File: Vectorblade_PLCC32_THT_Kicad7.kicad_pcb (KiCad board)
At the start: 2 copper layers, 47.2 x 46.9 mm, 12 parts, among them CON3 EDGE-CONNECTOR, U1 SST39SF020, U2 74AHC1G08, U3 74AHC1G04

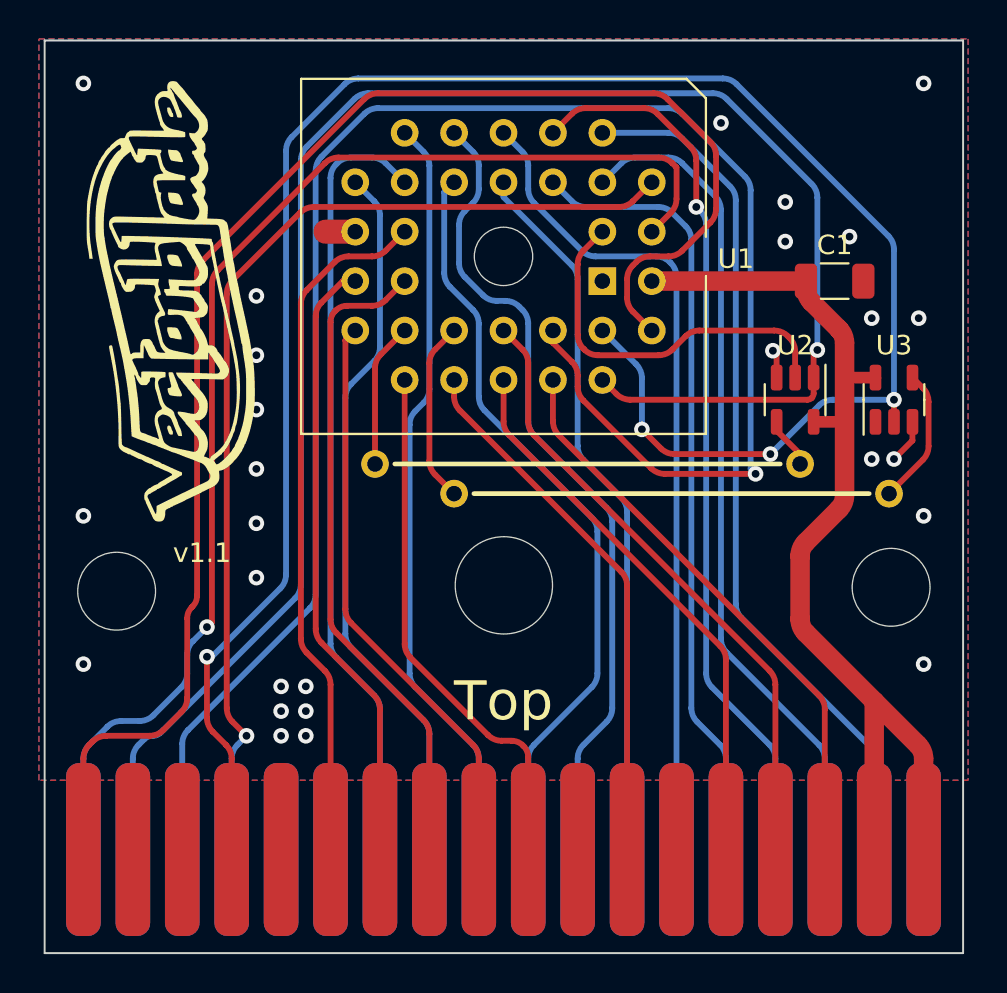
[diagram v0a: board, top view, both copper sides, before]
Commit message: Correct a roud track
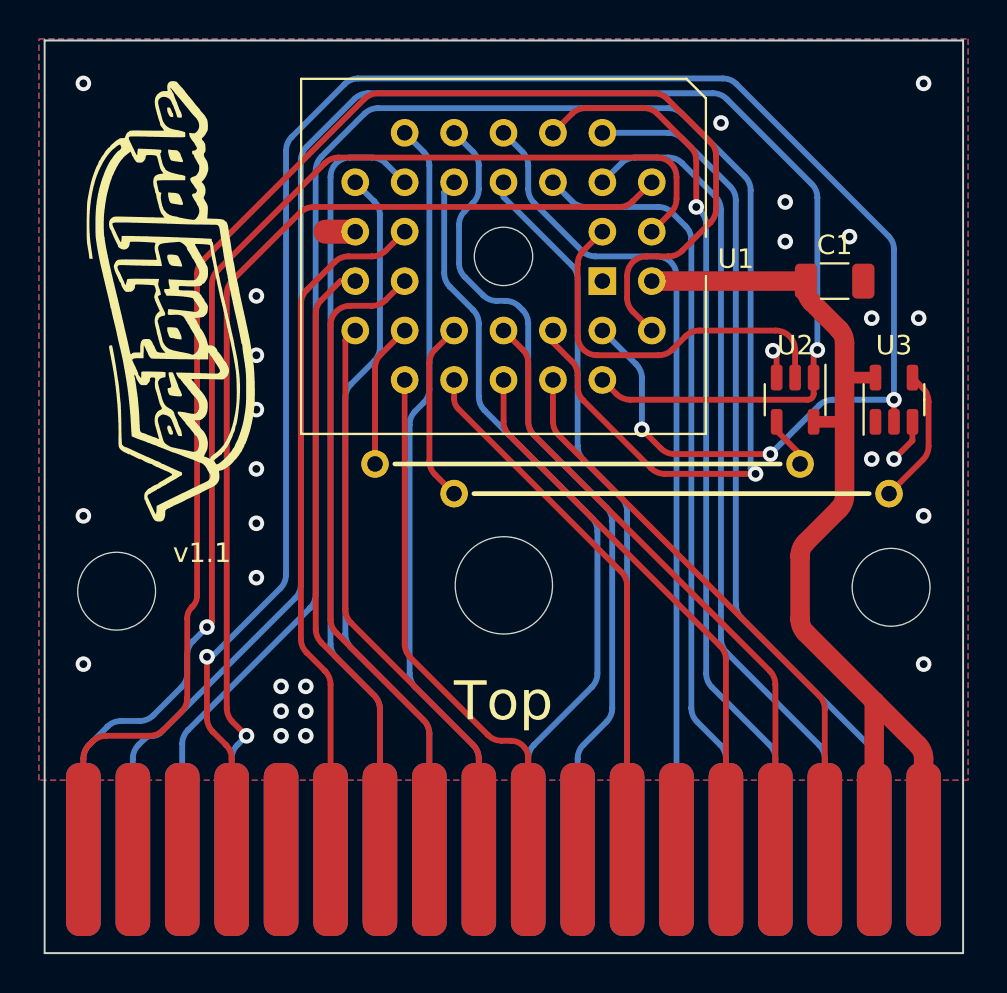
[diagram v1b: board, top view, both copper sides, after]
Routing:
- net /V-A13: track 92.5 -> 93.2 mm

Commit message: I forgot to connect A15
Shame !
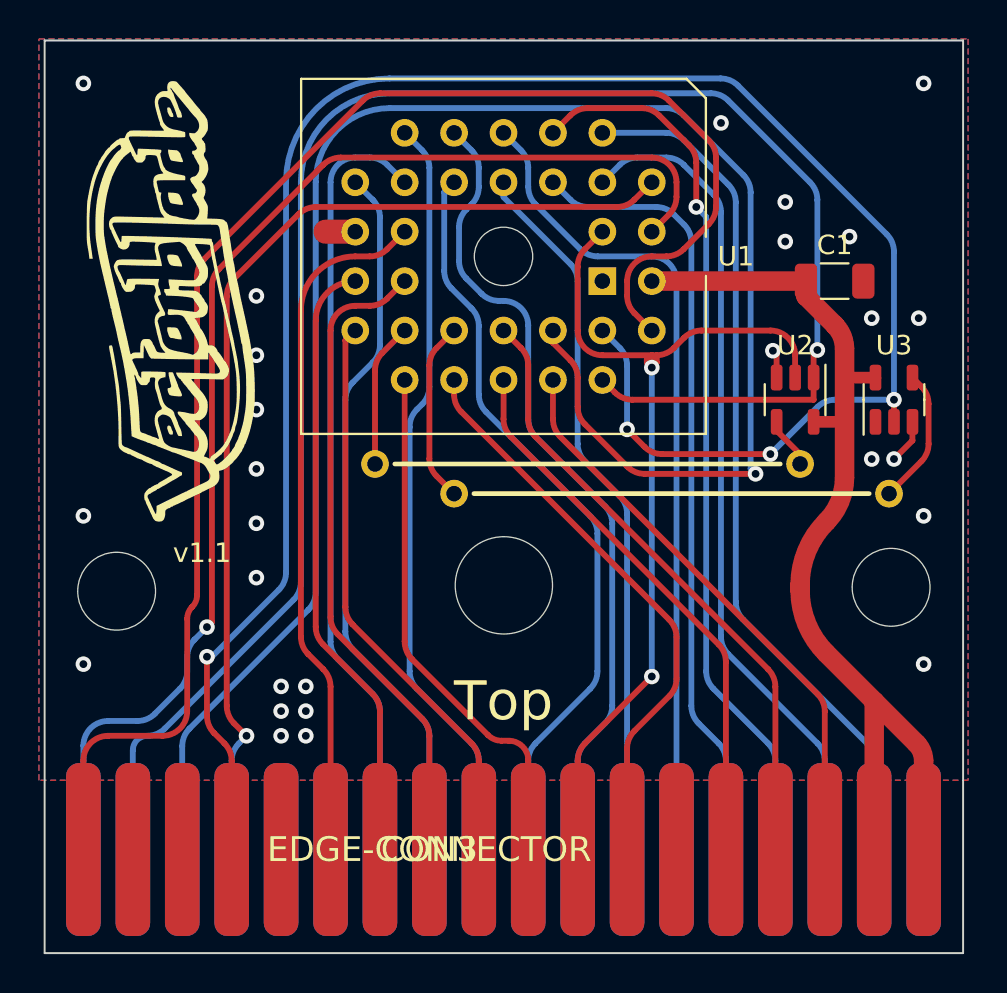
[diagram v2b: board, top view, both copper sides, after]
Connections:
- CON3 pad 16: unconnected-(CON3-Pad16) -> /V-A15
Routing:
- net /V-A15: track 19.9 -> 47.9 mm, vias 0 -> 2
- net /V-A10: track 27.7 -> 29.7 mm
